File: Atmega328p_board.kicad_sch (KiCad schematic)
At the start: 23 parts, among them U1 24LC1025, U2 24LC1025, U3 ATMEGA328P-AU, U4 DS1337S_, Y1 Crystal, Y2 Crystal

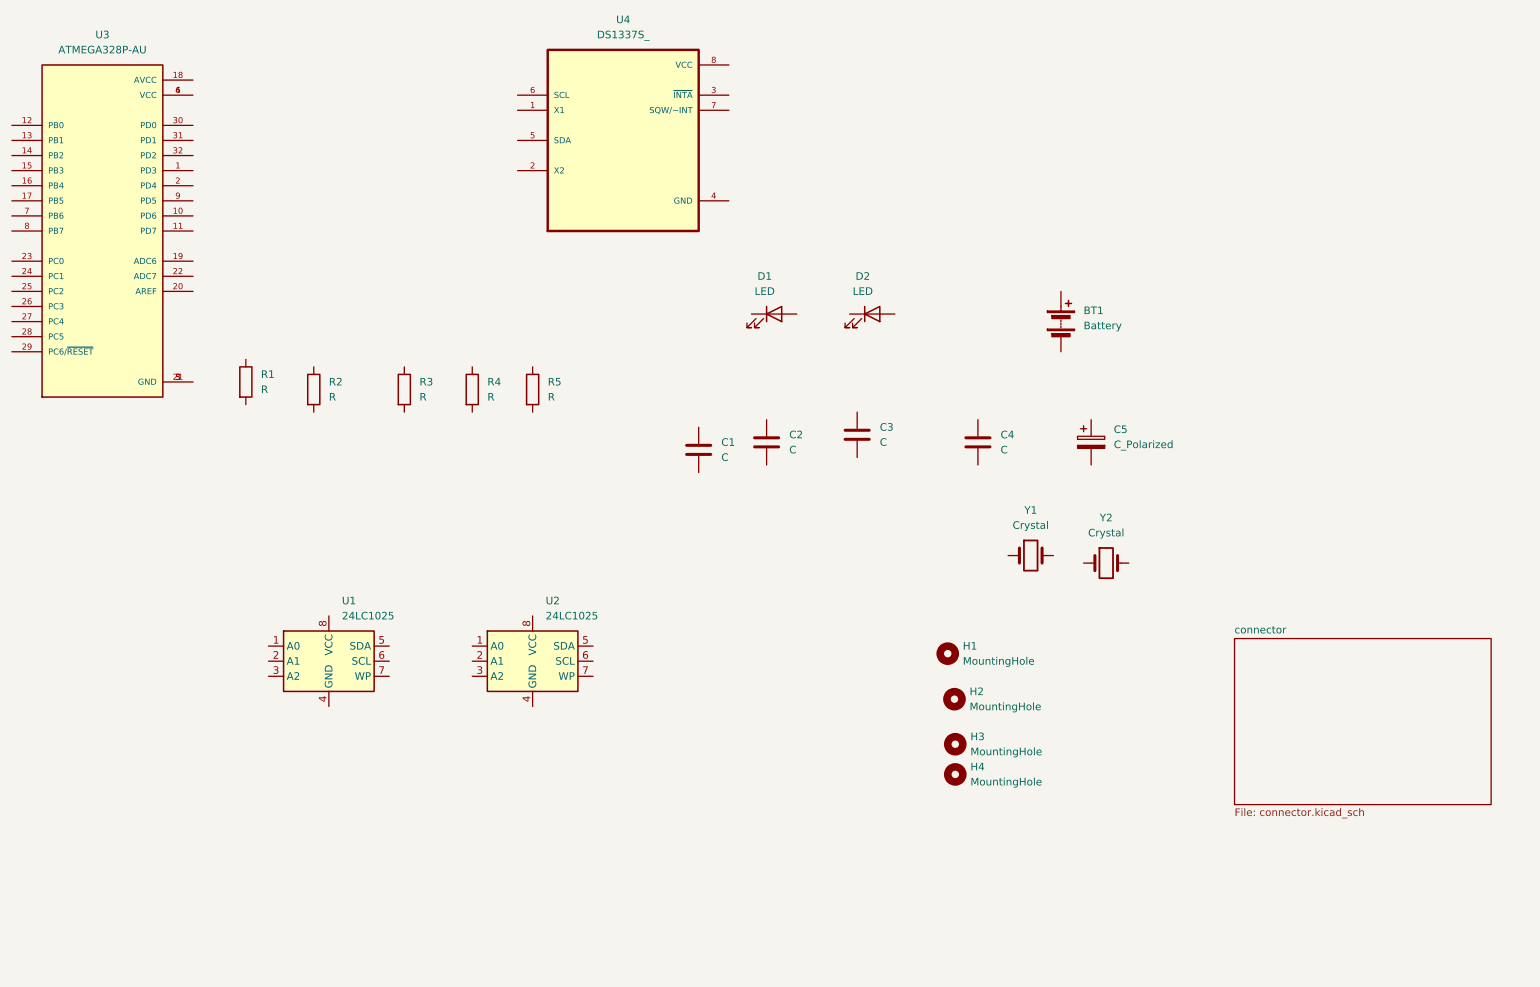
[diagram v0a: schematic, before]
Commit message: changed symbol position(arranged)
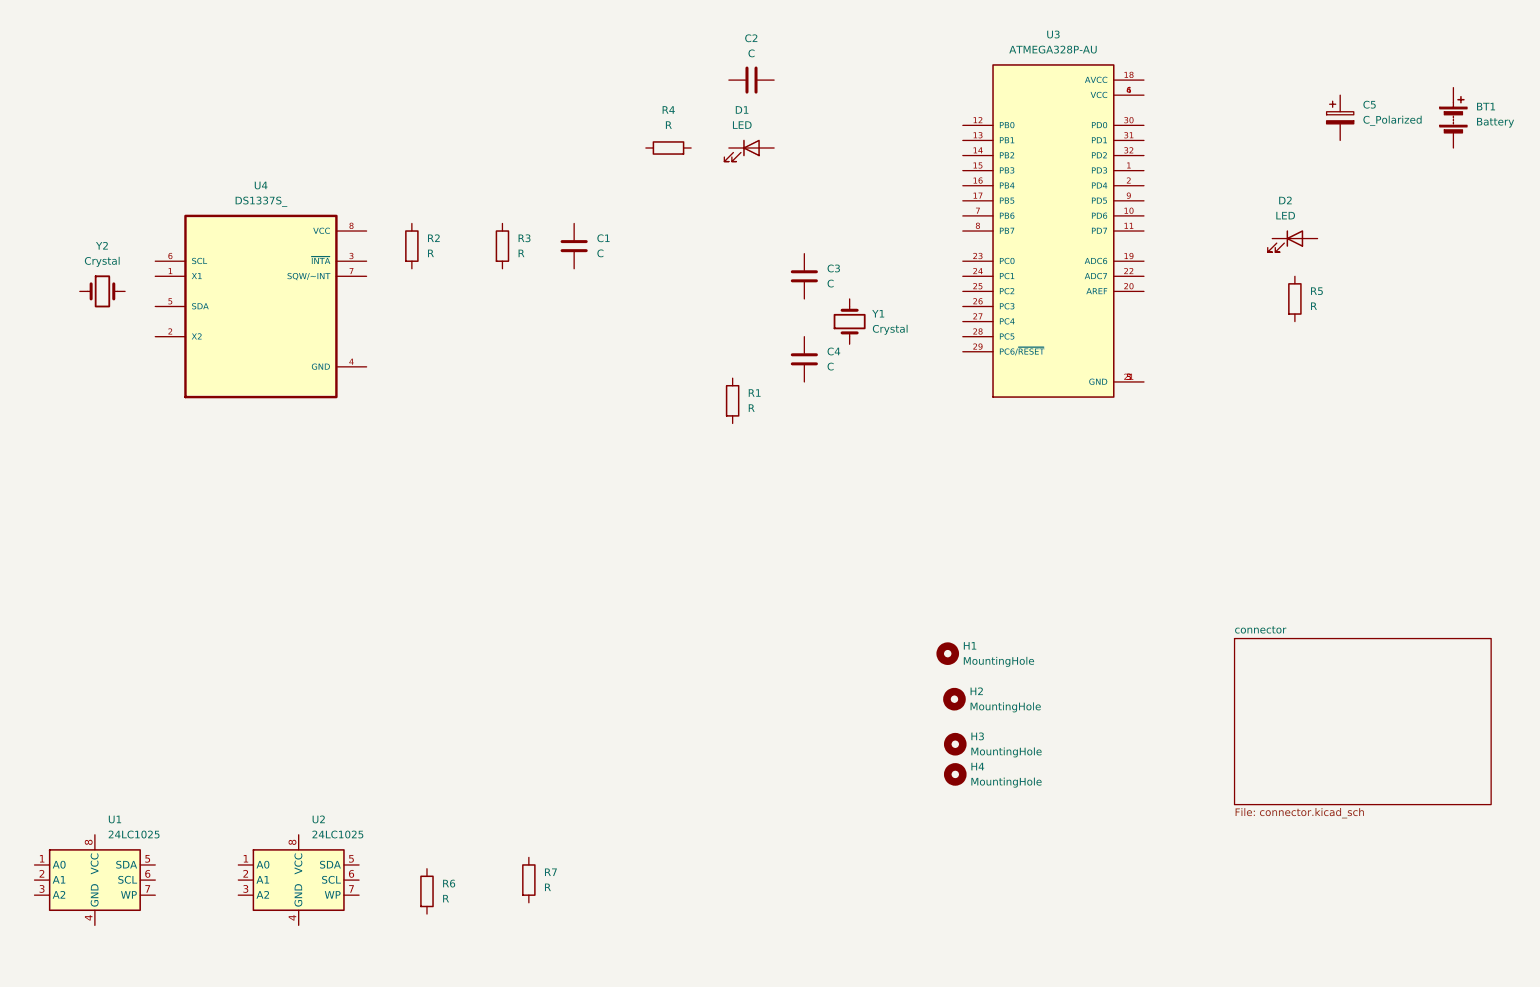
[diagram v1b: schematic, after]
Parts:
- added R6, R7: R, symbol Device:R
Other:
- moved on the sheet: BT1, C1, C2, C3, C4, C5, D1, D2, R2, R3, R4, R5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

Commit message: added values of all the components
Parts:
- C1, C2: value C -> 0.1uF
- C3, C4: value C -> 22pF
- C5: value C_Polarized -> 100nF
- R1, R2, R3: value R -> 10K
- R4, R5: value R -> 330
- R6, R7: value R -> 4.7K
- Y1: value Crystal -> 16MHz
- Y2: value Crystal -> 32.768 KHz
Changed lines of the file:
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@@
       (effects (font (size 1.27 1.27)))
     )
-    (property "Value" "C" (at 149.86 27.305 90)
+    (property "Value" "0.1uF" (at 149.86 27.305 90)
       (effects (font (size 1.27 1.27)))
     )
@@
     (property "Datasheet" "~" (at 149.86 31.75 0)
       (effects (font (size 1.27 1.27)) hide)
+    )
+    (property "purpose" "" (at 149.86 31.75 0)
+      (effects (font (size 1.27 1.27)))
     )
     (pin "1")
@@
       (effects (font (size 1.27 1.27)))
     )
-    (property "Value" "R" (at 135.89 39.37 90)
+    (property "Value" "330" (at 135.89 39.37 90)
       (effects (font (size 1.27 1.27)))
     )
@@
       (effects (font (size 1.27 1.27)) hide)
     )
+    (property "purpose" "" (at 135.89 43.18 0)
+      (effects (font (size 1.27 1.27)))
+    )
     (pin "2")
     (pin "1")
@@
       (effects (font (size 1.27 1.27)) (justify left))
     )
-    (property "Value" "R" (at 110.49 60.96 0)
+    (property "Value" "10K" (at 110.49 60.96 0)
       (effects (font (size 1.27 1.27)) (justify left))
     )
@@
       (effects (font (size 1.27 1.27)) hide)
     )
+    (property "purpose" "" (at 107.95 59.69 0)
+      (effects (font (size 1.27 1.27)))
+    )
     (pin "2")
     (pin "1")
@@
       (effects (font (size 1.27 1.27)) (justify left))
     )
-    (property "Value" "R" (at 97.79 169.545 0)
+    (property "Value" "4.7K" (at 97.79 169.545 0)
       (effects (font (size 1.27 1.27)) (justify left))
     )
@@
       (effects (font (size 1.27 1.27)))
     )
-    (property "Value" "Crystal" (at 40.64 62.23 0)
+    (property "Value" "32.768 KHz" (at 40.64 62.23 0)
       (effects (font (size 1.27 1.27)))
     )
@@
       (effects (font (size 1.27 1.27)) hide)
     )
+    (property "purpose" "" (at 40.64 67.31 0)
+      (effects (font (size 1.27 1.27)))
+    )
     (pin "2")
     (pin "1")
@@
   (symbol (lib_id "Device:R") (at 112.395 166.37 0) (unit 1)
     (in_bom yes) (on_board yes) (dnp no) (fields_autoplaced)
-    (property "Reference" "R7" (at 114.935 165.1 0)
-      (effects (font (size 1.27 1.27)) (justify left))
-    )
-    (property "Value" "R" (at 114.935 167.64 0)
+    (property "Reference" "R7" (at 114.3 165.1 0)
+      (effects (font (size 1.27 1.27)) (justify left))
+    )
+    (property "Value" "4.7K" (at 114.3 167.64 0)
       (effects (font (size 1.27 1.27)) (justify left))
     )
@@
       (effects (font (size 1.27 1.27)) (justify left))
     )
-    (property "Value" "C" (at 162.56 66.04 0)
+    (property "Value" "22pF" (at 162.56 66.04 0)
       (effects (font (size 1.27 1.27)) (justify left))
     )
@@
     (property "Datasheet" "~" (at 158.75 64.77 0)
       (effects (font (size 1.27 1.27)) hide)
+    )
+    (property "purpose" "" (at 158.75 64.77 0)
+      (effects (font (size 1.27 1.27)))
     )
     (pin "1")
@@
       (effects (font (size 1.27 1.27)) (justify left))
     )
-    (property "Value" "R" (at 243.84 69.85 0)
+    (property "Value" "330" (at 243.84 69.85 0)
       (effects (font (size 1.27 1.27)) (justify left))
     )
@@
     (property "Datasheet" "~" (at 241.3 68.58 0)
       (effects (font (size 1.27 1.27)) hide)
+    )
+    (property "purpose" "" (at 241.3 68.58 0)
+      (effects (font (size 1.27 1.27)))
     )
     (pin "2")
@@
       (effects (font (size 1.27 1.27)) (justify right))
     )
-    (property "Value" "Crystal" (at 170.18 73.66 90)
+    (property "Value" "16MHz" (at 170.18 73.66 90)
       (effects (font (size 1.27 1.27)) (justify right))
     )
@@
       (effects (font (size 1.27 1.27)) hide)
     )
+    (property "purpose" "" (at 166.37 72.39 0)
+      (effects (font (size 1.27 1.27)))
+    )
     (pin "2")
     (pin "1")
@@
       (effects (font (size 1.27 1.27)) (justify left))
     )
-    (property "Value" "R" (at 149.225 86.995 0)
+    (property "Value" "10K" (at 149.225 86.995 0)
       (effects (font (size 1.27 1.27)) (justify left))
     )
@@
       (effects (font (size 1.27 1.27)) hide)
     )
+    (property "purpose" "" (at 146.685 85.725 0)
+      (effects (font (size 1.27 1.27)))
+    )
     (pin "2")
     (pin "1")
@@
       (effects (font (size 1.27 1.27)) (justify left))
     )
-    (property "Value" "C" (at 123.825 60.96 0)
+    (property "Value" "0.1uF" (at 123.825 60.96 0)
       (effects (font (size 1.27 1.27)) (justify left))
     )
@@
       (effects (font (size 1.27 1.27)) hide)
     )
+    (property "purpose" "" (at 120.015 59.69 0)
+      (effects (font (size 1.27 1.27)))
+    )
     (pin "1")
     (pin "2")
@@
       (effects (font (size 1.27 1.27)) (justify left))
     )
-    (property "Value" "C_Polarized" (at 252.73 38.481 0)
+    (property "Value" "100nF" (at 252.73 38.481 0)
       (effects (font (size 1.27 1.27)) (justify left))
     )
@@
       (effects (font (size 1.27 1.27)) hide)
     )
+    (property "purpose" "" (at 248.92 38.1 0)
+      (effects (font (size 1.27 1.27)))
+    )
     (pin "1")
     (pin "2")
@@
       (effects (font (size 1.27 1.27)) (justify left))
     )
-    (property "Value" "C" (at 162.56 80.01 0)
+    (property "Value" "22pF" (at 162.56 80.01 0)
       (effects (font (size 1.27 1.27)) (justify left))
     )
@@
       (effects (font (size 1.27 1.27)) hide)
     )
+    (property "purpose" "" (at 158.75 78.74 0)
+      (effects (font (size 1.27 1.27)))
+    )
     (pin "1")
     (pin "2")
@@
       (effects (font (size 1.27 1.27)) (justify left))
     )
-    (property "Value" "R" (at 95.25 60.96 0)
+    (property "Value" "10K" (at 95.25 60.96 0)
       (effects (font (size 1.27 1.27)) (justify left))
     )
@@
       (effects (font (size 1.27 1.27)) hide)
     )
-    (pin "2")
+    (property "purpose" "" (at 92.71 59.69 0)
+      (effects (font (size 1.27 1.27)))
+    )
+    (pin "2")

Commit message: added footprints to all the symbol
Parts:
- BT1: footprint (none) -> Connector_PinHeader_2.54mm:PinHeader_1x02_P2.54mm_Vertical
- C1, C2, C3, C4, C5: footprint (none) -> Capacitor_SMD:C_0805_2012Metric
- D1, D2: footprint (none) -> LED_SMD:LED_0805_2012Metric
- H1, H2, H3, H4: footprint (none) -> MountingHole:MountingHole_2.1mm
- R1, R2, R3, R4, R5, R6, R7: footprint (none) -> Resistor_SMD:R_0805_2012Metric
- U1, U2: footprint (none) -> Package_SO:SOIC-8_5.275x5.275mm_P1.27mm
- Y1, Y2: footprint (none) -> Crystal:Crystal_SMD_5032-2Pin_5.0x3.2mm_HandSoldering
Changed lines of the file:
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@@
       (effects (font (size 1.27 1.27)) (justify left))
     )
-    (property "Footprint" "" (at 184.15 143.51 0)
+    (property "Footprint" "MountingHole:MountingHole_2.1mm" (at 184.15 143.51 0)
       (effects (font (size 1.27 1.27)) hide)
     )
@@
       (effects (font (size 1.27 1.27)))
     )
-    (property "Footprint" "" (at 153.67 30.7848 0)
+    (property "Footprint" "Capacitor_SMD:C_0805_2012Metric" (at 153.67 30.7848 0)
       (effects (font (size 1.27 1.27)) hide)
     )
@@
       (effects (font (size 1.27 1.27)) (justify left))
     )
-    (property "Footprint" "" (at 73.66 166.37 0)
+    (property "Footprint" "Package_SO:SOIC-8_5.275x5.275mm_P1.27mm" (at 73.66 166.37 0)
       (effects (font (size 1.27 1.27)) hide)
     )
@@
       (effects (font (size 1.27 1.27)))
     )
-    (property "Footprint" "" (at 135.89 44.958 90)
+    (property "Footprint" "Resistor_SMD:R_0805_2012Metric" (at 135.89 44.958 90)
       (effects (font (size 1.27 1.27)) hide)
     )
@@
       (effects (font (size 1.27 1.27)) (justify left))
     )
-    (property "Footprint" "" (at 106.172 59.69 90)
+    (property "Footprint" "Resistor_SMD:R_0805_2012Metric" (at 106.172 59.69 90)
       (effects (font (size 1.27 1.27)) hide)
     )
@@
       (effects (font (size 1.27 1.27)) (justify left))
     )
-    (property "Footprint" "" (at 93.472 168.275 90)
+    (property "Footprint" "Resistor_SMD:R_0805_2012Metric" (at 93.472 168.275 90)
       (effects (font (size 1.27 1.27)) hide)
     )
@@
       (effects (font (size 1.27 1.27)) (justify left))
     )
-    (property "Footprint" "" (at 267.97 36.576 90)
+    (property "Footprint" "Connector_PinHeader_2.54mm:PinHeader_1x02_P2.54mm_Vertical" (at 267.97 36.576 90)
       (effects (font (size 1.27 1.27)) hide)
     )
@@
       (effects (font (size 1.27 1.27)))
     )
-    (property "Footprint" "" (at 241.3 58.42 0)
+    (property "Footprint" "LED_SMD:LED_0805_2012Metric" (at 241.3 58.42 0)
       (effects (font (size 1.27 1.27)) hide)
     )
@@
       (effects (font (size 1.27 1.27)) (justify left))
     )
-    (property "Footprint" "" (at 184.15 148.59 0)
+    (property "Footprint" "MountingHole:MountingHole_2.1mm" (at 184.15 148.59 0)
       (effects (font (size 1.27 1.27)) hide)
     )
@@
       (effects (font (size 1.27 1.27)) (justify left))
     )
-    (property "Footprint" "" (at 39.37 166.37 0)
+    (property "Footprint" "Package_SO:SOIC-8_5.275x5.275mm_P1.27mm" (at 39.37 166.37 0)
       (effects (font (size 1.27 1.27)) hide)
     )
@@
       (effects (font (size 1.27 1.27)))
     )
-    (property "Footprint" "" (at 40.64 67.31 0)
+    (property "Footprint" "Crystal:Crystal_SMD_5032-2Pin_5.0x3.2mm_HandSoldering" (at 40.64 67.31 0)
       (effects (font (size 1.27 1.27)) hide)
     )
@@
       (effects (font (size 1.27 1.27)) (justify left))
     )
-    (property "Footprint" "" (at 110.617 166.37 90)
+    (property "Footprint" "Resistor_SMD:R_0805_2012Metric" (at 110.617 166.37 90)
       (effects (font (size 1.27 1.27)) hide)
     )
@@
       (effects (font (size 1.27 1.27)) (justify left))
     )
-    (property "Footprint" "" (at 184.0114 135.931 0)
+    (property "Footprint" "MountingHole:MountingHole_2.1mm" (at 184.0114 135.931 0)
       (effects (font (size 1.27 1.27)) hide)
     )
@@
       (effects (font (size 1.27 1.27)) (justify left))
     )
-    (property "Footprint" "" (at 159.7152 68.58 0)
+    (property "Footprint" "Capacitor_SMD:C_0805_2012Metric" (at 159.7152 68.58 0)
       (effects (font (size 1.27 1.27)) hide)
     )
@@
       (effects (font (size 1.27 1.27)) (justify left))
     )
-    (property "Footprint" "" (at 182.88 128.27 0)
+    (property "Footprint" "MountingHole:MountingHole_2.1mm" (at 182.88 128.27 0)
       (effects (font (size 1.27 1.27)) hide)
     )
@@
       (effects (font (size 1.27 1.27)))
     )
-    (property "Footprint" "" (at 149.86 43.18 0)
+    (property "Footprint" "LED_SMD:LED_0805_2012Metric" (at 149.86 43.18 0)
       (effects (font (size 1.27 1.27)) hide)
     )
@@
       (effects (font (size 1.27 1.27)) (justify left))
     )
-    (property "Footprint" "" (at 239.522 68.58 90)
+    (property "Footprint" "Resistor_SMD:R_0805_2012Metric" (at 239.522 68.58 90)
       (effects (font (size 1.27 1.27)) hide)
     )
@@
       (effects (font (size 1.27 1.27)) (justify right))
     )
-    (property "Footprint" "" (at 166.37 72.39 0)
+    (property "Footprint" "Crystal:Crystal_SMD_5032-2Pin_5.0x3.2mm_HandSoldering" (at 166.37 72.39 0)
       (effects (font (size 1.27 1.27)) hide)
     )
@@
       (effects (font (size 1.27 1.27)) (justify left))
     )
-    (property "Footprint" "" (at 144.907 85.725 90)
+    (property "Footprint" "Resistor_SMD:R_0805_2012Metric" (at 144.907 85.725 90)
       (effects (font (size 1.27 1.27)) hide)
     )
@@
       (effects (font (size 1.27 1.27)) (justify left))
     )
-    (property "Footprint" "" (at 120.9802 63.5 0)
+    (property "Footprint" "Capacitor_SMD:C_0805_2012Metric" (at 120.9802 63.5 0)
       (effects (font (size 1.27 1.27)) hide)
     )
@@
       (effects (font (size 1.27 1.27)) (justify left))
     )
-    (property "Footprint" "" (at 249.8852 41.91 0)
+    (property "Footprint" "Capacitor_SMD:C_0805_2012Metric" (at 249.8852 41.91 0)
       (effects (font (size 1.27 1.27)) hide)
     )
@@
       (effects (font (size 1.27 1.27)) (justify left))
     )
-    (property "Footprint" "" (at 159.7152 82.55 0)
+    (property "Footprint" "Capacitor_SMD:C_0805_2012Metric" (at 159.7152 82.55 0)
       (effects (font (size 1.27 1.27)) hide)
     )
@@
       (effects (font (size 1.27 1.27)) (justify left))
     )
-    (property "Footprint" "" (at 90.932 59.69 90)
-      (effects (font (size 1.27 1.27)) hide)
-    )
+    (property "Footprint" "Resistor_SMD:R_0805_2012Metric" (at 90.932 59.69 90)
+      (effects (font (size 1.27 1.27)) hide)
+    )
